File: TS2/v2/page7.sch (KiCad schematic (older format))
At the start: 9 parts, among them P1 FTDI (TERMINAL), P2 FTDI (HOST), U29 6850, U3 74LS00, U30 6850, U31 MC14411, U5 74LS04, Y1 1.842MHz

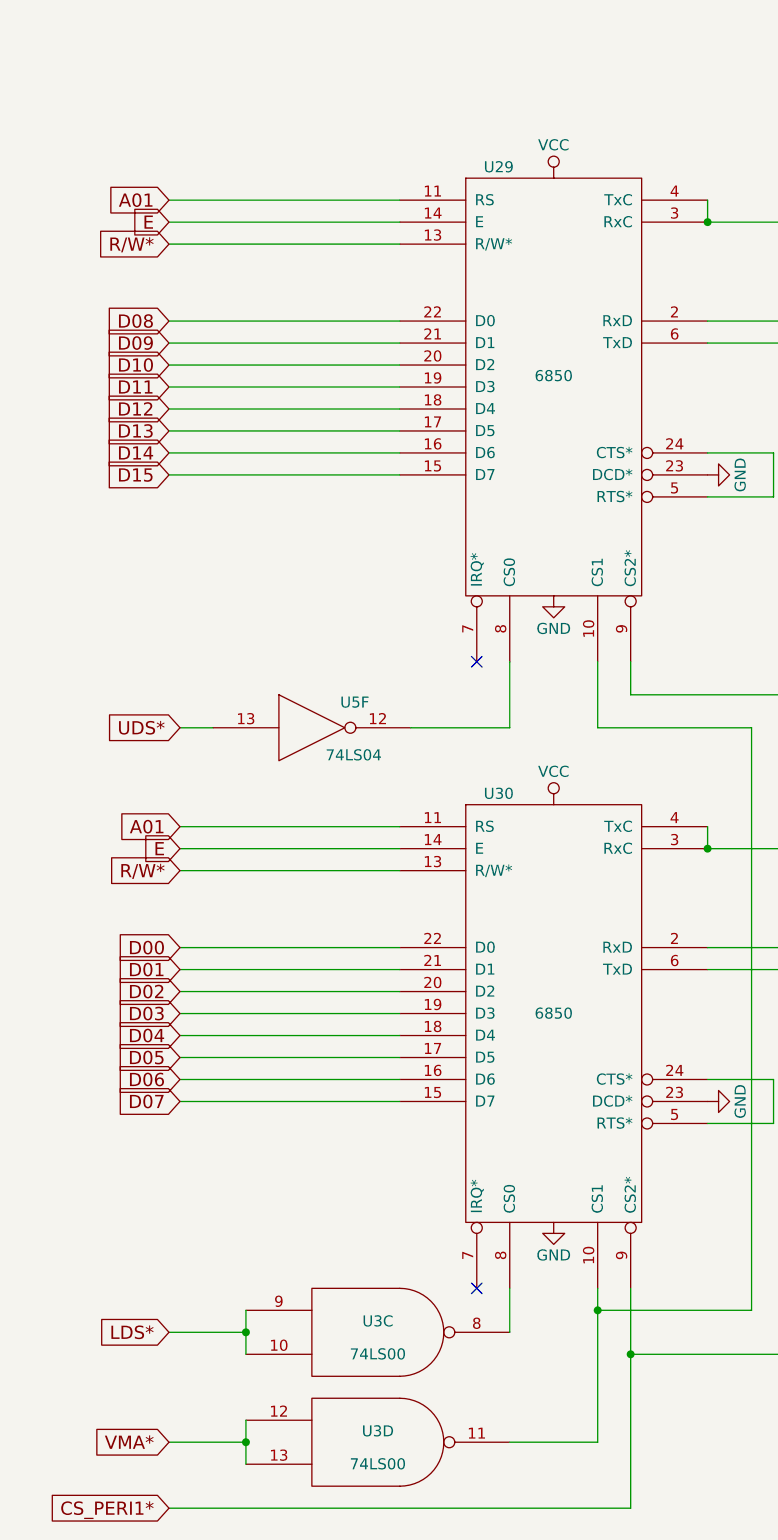
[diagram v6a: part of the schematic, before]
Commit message: Swap two chips to make circuit more symmetical. Move labels on 6850s.
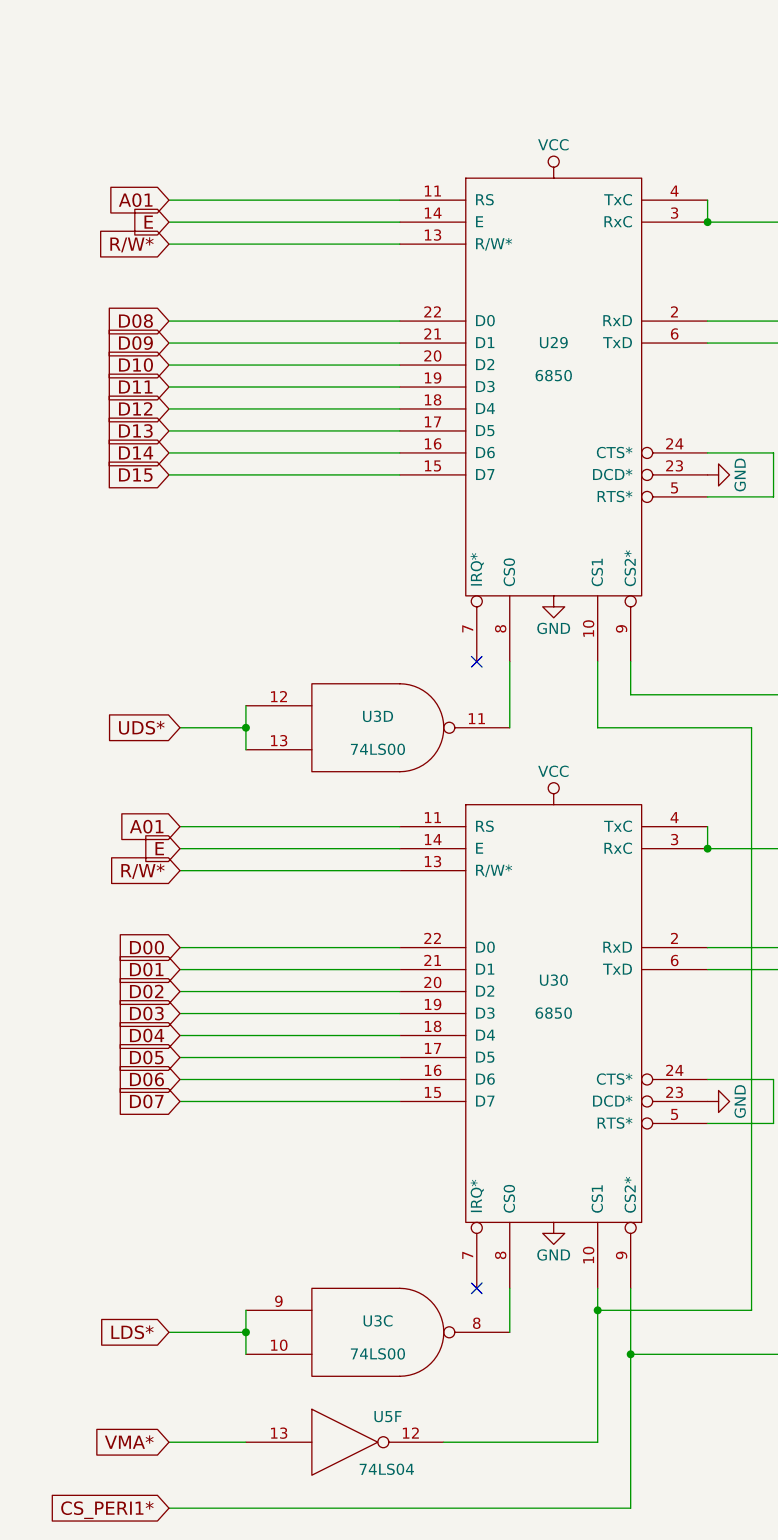
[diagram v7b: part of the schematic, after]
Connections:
- net UDS*: now also U3.12, U3.13; no longer U5.13
- net VMA*: now also U5.13; no longer U3.12, U3.13
- net at U29.10 (CS1), U30.10 (CS1): now also U5.12; no longer U3.11
- net at U29.8 (CS0): now also U3.11; no longer U5.12
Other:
- moved on the sheet: U3D, U5F
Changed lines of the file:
@@
 U 1 1 57C6575D
 P 3800 2600
-F 0 "U29" H 3550 3600 50  0000 C CNN
+F 0 "U29" H 3800 2800 50  0000 C CNN
 F 1 "6850" H 3800 2650 50  0000 C CNN
 F 2 "" H 3800 2600 50  0000 C CNN
@@
 U 1 1 57C657EF
 P 3800 5450
-F 0 "U30" H 3550 6450 50  0000 C CNN
+F 0 "U30" H 3800 5600 50  0000 C CNN
 F 1 "6850" H 3800 5450 50  0000 C CNN
 F 2 "" H 3800 5450 50  0000 C CNN
@@
 L 74LS04 U5
 U 6 1 57C69631
-P 2700 4150
-F 0 "U5" H 2895 4265 50  0000 C CNN
-F 1 "74LS04" H 2890 4025 50  0000 C CNN
-F 2 "" H 2700 4150 50  0000 C CNN
-F 3 "" H 2700 4150 50  0000 C CNN
-	6    2700 4150
+P 2850 7400
+F 0 "U5" H 3045 7515 50  0000 C CNN
+F 1 "74LS04" H 3040 7275 50  0000 C CNN
+F 2 "" H 2850 7400 50  0000 C CNN
+F 3 "" H 2850 7400 50  0000 C CNN
+	6    2850 7400
 	1    0    0    -1
 $EndComp
@@
 	4150 7700 2050 7700
 Wire Wire Line
-	3150 4150 3600 4150
-Wire Wire Line
 	3600 4150 3600 3850
 Wire Wire Line
-	2100 4150 2250 4150
+	2100 4150 2400 4150
 Wire Wire Line
 	4000 3850 4000 4150
@@
 L 74LS00 U3
 U 4 1 5842F155
-P 3000 7400
-F 0 "U3" H 3000 7450 50  0000 C CNN
-F 1 "74LS00" H 3000 7300 50  0000 C CNN
-F 2 "" H 3000 7400 50  0000 C CNN
-F 3 "" H 3000 7400 50  0000 C CNN
-	4    3000 7400
+P 3000 4150
+F 0 "U3" H 3000 4200 50  0000 C CNN
+F 1 "74LS00" H 3000 4050 50  0000 C CNN
+F 2 "" H 3000 4150 50  0000 C CNN
+F 3 "" H 3000 4150 50  0000 C CNN
+	4    3000 4150
 	1    0    0    -1
 $EndComp
@@
 Connection ~ 2400 6900
 Wire Wire Line
-	4000 6700 4000 7400
-Wire Wire Line
-	4000 7400 3600 7400
-Wire Wire Line
-	2400 7300 2400 7500
+	4000 7400 4000 6700
+Wire Wire Line
+	3300 7400 4000 7400
 Wire Wire Line
 	2400 7400 2050 7400
-Connection ~ 2400 7400
+Wire Wire Line
+	2400 4050 2400 4250
+Connection ~ 2400 4150
 $EndSCHEMATC
